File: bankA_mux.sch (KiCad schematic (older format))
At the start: 6 parts, among them U10 SHIFTER, U9 74HC4051

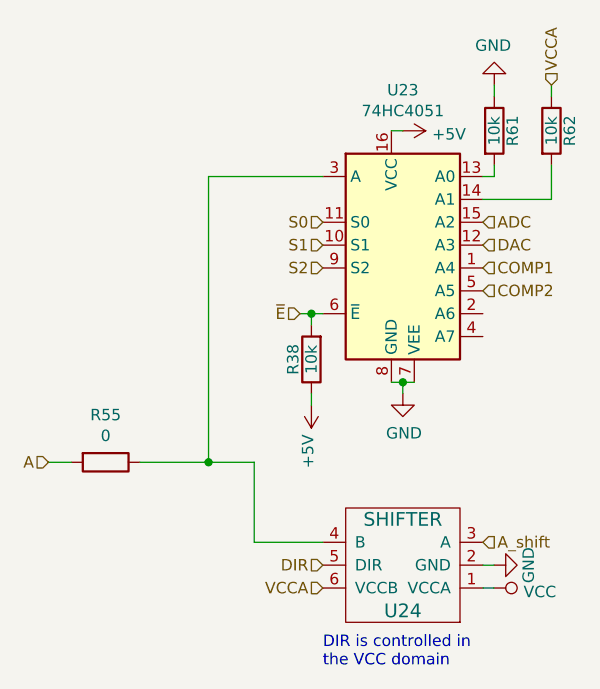
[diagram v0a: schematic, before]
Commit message: Changed headers for bank A and B, combined ADC voltage divider / pull-ups
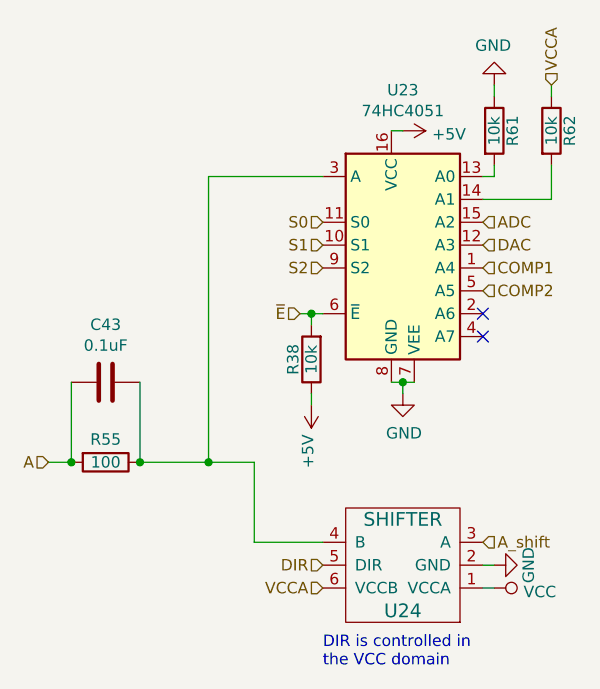
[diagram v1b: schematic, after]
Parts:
- added C39: 0.1uF, gsg-modules:0402, symbol Device:C
- R48: value 0 -> 100; Description (none) -> RES 100 OHM 5% 1/16W 0402; Manufacturer (none) -> Stackpole Electronics Inc; Part Number (none) -> RMCF0402JT100R
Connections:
- net A: now also C39.1
- net at R48.1, U10.4 (B), U9.3 (A): now also C39.2
- no-connect marks 0 -> 2
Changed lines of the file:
@@
 $Descr A4 11693 8268
 encoding utf-8
-Sheet 4 9
+Sheet 5 10
 Title ""
 Date ""
@@
 AR Path="/5D190D22/5CB0C423" Ref="R51"  Part="1"
 AR Path="/5D1A466A/5CB0C423" Ref="R53"  Part="1"
-F 0 "R55" V 2593 3700 50  0000 C CNN
-F 1 "0" V 2684 3700 50  0000 C CNN
+F 0 "R55" V 2700 3700 50  0000 C CNN
+F 1 "100" V 2800 3700 50  0000 C CNN
 F 2 "gsg-modules:0402" V 2730 3700 50  0001 C CNN
 F 3 "~" H 2800 3700 50  0001 C CNN
+F 4 "Stackpole Electronics Inc" H 2800 3700 50  0001 C CNN "Manufacturer"
+F 5 "RMCF0402JT100R" H 2800 3700 50  0001 C CNN "Part Number"
+F 6 "RES 100 OHM 5% 1/16W 0402" H 2800 3700 50  0001 C CNN "Description"
 	1    2800 3700
 	0    1    1    0
@@
 	1    0    0    -1
 $EndComp
+NoConn ~ 4450 3050
+NoConn ~ 4450 3150
+$Comp
+L Device:C C39
+U 1 1 5D112AA5
+P 2800 3350
+AR Path="/5D190D22/5D112AA5" Ref="C39"  Part="1"
+AR Path="/5D1A466A/5D112AA5" Ref="C41"  Part="1"
+AR Path="/5D190D0C/5D112AA5" Ref="C38"  Part="1"
+AR Path="/5CF421CD/5D112AA5" Ref="C20"  Part="1"
+AR Path="/5D17D622/5D112AA5" Ref="C37"  Part="1"
+AR Path="/5D1A4654/5D112AA5" Ref="C40"  Part="1"
+AR Path="/5D1A4680/5D112AA5" Ref="C42"  Part="1"
+AR Path="/5D1A4696/5D112AA5" Ref="C43"  Part="1"
+F 0 "C43" V 3052 3350 50  0000 C CNN
+F 1 "0.1uF" V 2961 3350 50  0000 C CNN
+F 2 "gsg-modules:0402" H 2838 3200 50  0001 C CNN
+F 3 "~" H 2800 3350 50  0001 C CNN
+F 4 "Taiyo Yuden" H 2800 3350 50  0001 C CNN "Manufacturer"
+F 5 "EMK105BJ104KV-F" H 2800 3350 50  0001 C CNN "Part Number"
+F 6 "CAP CER 0.1UF 16V X5R 0402 " H 2800 3350 50  0001 C CNN "Description"
+	1    2800 3350
+	0    -1   -1   0
+$EndComp
+Wire Wire Line
+	2650 3700 2650 3350
+Connection ~ 2650 3700
+Wire Wire Line
+	2950 3350 2950 3700
+Connection ~ 2950 3700
 $EndSCHEMATC

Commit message: Completed routing of new connectors.
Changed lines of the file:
@@
 $Descr A4 11693 8268
 encoding utf-8
-Sheet 5 10
+Sheet 5 17
 Title ""
 Date ""
@@
 AR Path="/5D1A4680/5CF3E254" Ref="U21"  Part="1"
 AR Path="/5D1A4696/5CF3E254" Ref="U23"  Part="1"
-F 0 "U23" H 4100 3428 50  0000 C CNN
+F 0 "U11" H 4100 3428 50  0000 C CNN
 F 1 "74HC4051" H 4100 3337 50  0000 C CNN
 F 2 "Package_TO_SOT_SMD:SOT-763-1" H 4050 2350 50  0001 C CNN
@@
 AR Path="/5D1A4680/5CF3E25C" Ref="#PWR0180"  Part="1"
 AR Path="/5D1A4696/5CF3E25C" Ref="#PWR0186"  Part="1"
-F 0 "#PWR0186" H 4100 2100 50  0001 C CNN
+F 0 "#PWR0150" H 4100 2100 50  0001 C CNN
 F 1 "+5V" V 4115 2378 50  0000 L CNN
 F 2 "" H 4100 2250 50  0001 C CNN
@@
 AR Path="/5D1A4680/5CF3E263" Ref="#PWR0181"  Part="1"
 AR Path="/5D1A4696/5CF3E263" Ref="#PWR0187"  Part="1"
-F 0 "#PWR0187" H 4100 3150 50  0001 C CNN
+F 0 "#PWR0151" H 4100 3150 50  0001 C CNN
 F 1 "GND" H 4105 3227 50  0000 C CNN
 F 2 "" H 4100 3400 50  0001 C CNN
@@
 AR Path="/5D1A4680/5CF3E282" Ref="#PWR0182"  Part="1"
 AR Path="/5D1A4696/5CF3E282" Ref="#PWR0188"  Part="1"
-F 0 "#PWR0188" H 4500 1800 50  0001 C CNN
+F 0 "#PWR0152" H 4500 1800 50  0001 C CNN
 F 1 "GND" H 4505 1877 50  0000 C CNN
 F 2 "" H 4500 2050 50  0001 C CNN
@@
 AR Path="/5D1A4680/5CF3E28C" Ref="U22"  Part="1"
 AR Path="/5D1A4696/5CF3E28C" Ref="U24"  Part="1"
-F 0 "U24" H 4100 4350 60  0000 C CNN
+F 0 "U12" H 4100 4350 60  0000 C CNN
 F 1 "SHIFTER" H 4100 3950 60  0000 C CNN
 F 2 "gsg-modules:SOT363" H 4100 4150 60  0001 C CNN
@@
 AR Path="/5D1A4680/5CF3E293" Ref="#PWR0183"  Part="1"
 AR Path="/5D1A4696/5CF3E293" Ref="#PWR0189"  Part="1"
-F 0 "#PWR0189" H 4500 3900 50  0001 C CNN
+F 0 "#PWR0153" H 4500 3900 50  0001 C CNN
 F 1 "GND" H 4500 4000 50  0000 C CNN
 F 2 "" H 4500 4150 60  0000 C CNN
@@
 AR Path="/5D1A4680/5CF3E2A6" Ref="R35"  Part="1"
 AR Path="/5D1A4696/5CF3E2A6" Ref="R38"  Part="1"
-F 0 "R38" V 3780 3250 50  0000 C CNN
+F 0 "R20" V 3780 3250 50  0000 C CNN
 F 1 "10k" V 3700 3250 50  0000 C CNN
 F 2 "gsg-modules:0402" V 3630 3250 50  0001 C CNN
@@
 AR Path="/5D1A4680/5CF3E2B2" Ref="#PWR0184"  Part="1"
 AR Path="/5D1A4696/5CF3E2B2" Ref="#PWR0190"  Part="1"
-F 0 "#PWR0190" H 3700 3300 50  0001 C CNN
+F 0 "#PWR0154" H 3700 3300 50  0001 C CNN
 F 1 "+5V" V 3715 3578 50  0000 L CNN
 F 2 "" H 3700 3450 50  0001 C CNN
@@
 AR Path="/5D1A4680/5CF3E2B8" Ref="#PWR0185"  Part="1"
 AR Path="/5D1A4696/5CF3E2B8" Ref="#PWR0191"  Part="1"
-F 0 "#PWR0191" H 4500 4100 50  0001 C CNN
+F 0 "#PWR0155" H 4500 4100 50  0001 C CNN
 F 1 "VCC" V 4517 4378 50  0000 L CNN
 F 2 "" H 4500 4250 50  0001 C CNN
@@
 AR Path="/5D190D22/5CB0C423" Ref="R51"  Part="1"
 AR Path="/5D1A466A/5CB0C423" Ref="R53"  Part="1"
-F 0 "R55" V 2700 3700 50  0000 C CNN
+F 0 "R49" V 2700 3700 50  0000 C CNN
 F 1 "100" V 2800 3700 50  0000 C CNN
 F 2 "gsg-modules:0402" V 2730 3700 50  0001 C CNN
@@
 AR Path="/5D1A4680/5CDC112C" Ref="R47"  Part="1"
 AR Path="/5D1A4696/5CDC112C" Ref="R62"  Part="1"
-F 0 "R62" V 4830 2250 50  0000 C CNN
+F 0 "R28" V 4830 2250 50  0000 C CNN
 F 1 "10k" V 4750 2250 50  0000 C CNN
 F 2 "gsg-modules:0402" V 4680 2250 50  0001 C CNN
@@
 AR Path="/5D1A4680/5CDC1279" Ref="R46"  Part="1"
 AR Path="/5D1A4696/5CDC1279" Ref="R61"  Part="1"
-F 0 "R61" V 4580 2250 50  0000 C CNN
+F 0 "R27" V 4580 2250 50  0000 C CNN
 F 1 "10k" V 4500 2250 50  0000 C CNN
 F 2 "gsg-modules:0402" V 4430 2250 50  0001 C CNN
@@
 AR Path="/5D1A4680/5D112AA5" Ref="C42"  Part="1"
 AR Path="/5D1A4696/5D112AA5" Ref="C43"  Part="1"
-F 0 "C43" V 3052 3350 50  0000 C CNN
+F 0 "C37" V 3052 3350 50  0000 C CNN
 F 1 "0.1uF" V 2961 3350 50  0000 C CNN
 F 2 "gsg-modules:0402" H 2838 3200 50  0001 C CNN

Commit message: Completed Bank A mux routing.
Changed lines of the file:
@@
 AR Path="/5D1A4680/5CF3E254" Ref="U21"  Part="1"
 AR Path="/5D1A4696/5CF3E254" Ref="U23"  Part="1"
-F 0 "U11" H 4100 3428 50  0000 C CNN
+F 0 "U19" H 4100 3428 50  0000 C CNN
 F 1 "74HC4051" H 4100 3337 50  0000 C CNN
 F 2 "Package_TO_SOT_SMD:SOT-763-1" H 4050 2350 50  0001 C CNN
@@
 AR Path="/5D1A4680/5CF3E25C" Ref="#PWR0180"  Part="1"
 AR Path="/5D1A4696/5CF3E25C" Ref="#PWR0186"  Part="1"
-F 0 "#PWR0150" H 4100 2100 50  0001 C CNN
+F 0 "#PWR0186" H 4100 2100 50  0001 C CNN
 F 1 "+5V" V 4115 2378 50  0000 L CNN
 F 2 "" H 4100 2250 50  0001 C CNN
@@
 AR Path="/5D1A4680/5CF3E263" Ref="#PWR0181"  Part="1"
 AR Path="/5D1A4696/5CF3E263" Ref="#PWR0187"  Part="1"
-F 0 "#PWR0151" H 4100 3150 50  0001 C CNN
+F 0 "#PWR0187" H 4100 3150 50  0001 C CNN
 F 1 "GND" H 4105 3227 50  0000 C CNN
 F 2 "" H 4100 3400 50  0001 C CNN
@@
 AR Path="/5D1A4680/5CF3E282" Ref="#PWR0182"  Part="1"
 AR Path="/5D1A4696/5CF3E282" Ref="#PWR0188"  Part="1"
-F 0 "#PWR0152" H 4500 1800 50  0001 C CNN
+F 0 "#PWR0188" H 4500 1800 50  0001 C CNN
 F 1 "GND" H 4505 1877 50  0000 C CNN
 F 2 "" H 4500 2050 50  0001 C CNN
@@
 AR Path="/5D1A4680/5CF3E28C" Ref="U22"  Part="1"
 AR Path="/5D1A4696/5CF3E28C" Ref="U24"  Part="1"
-F 0 "U12" H 4100 4350 60  0000 C CNN
+F 0 "U20" H 4100 4350 60  0000 C CNN
 F 1 "SHIFTER" H 4100 3950 60  0000 C CNN
 F 2 "gsg-modules:SOT363" H 4100 4150 60  0001 C CNN
@@
 AR Path="/5D1A4680/5CF3E293" Ref="#PWR0183"  Part="1"
 AR Path="/5D1A4696/5CF3E293" Ref="#PWR0189"  Part="1"
-F 0 "#PWR0153" H 4500 3900 50  0001 C CNN
+F 0 "#PWR0189" H 4500 3900 50  0001 C CNN
 F 1 "GND" H 4500 4000 50  0000 C CNN
 F 2 "" H 4500 4150 60  0000 C CNN
@@
 AR Path="/5D1A4680/5CF3E2A6" Ref="R35"  Part="1"
 AR Path="/5D1A4696/5CF3E2A6" Ref="R38"  Part="1"
-F 0 "R20" V 3780 3250 50  0000 C CNN
+F 0 "R32" V 3780 3250 50  0000 C CNN
 F 1 "10k" V 3700 3250 50  0000 C CNN
 F 2 "gsg-modules:0402" V 3630 3250 50  0001 C CNN
@@
 AR Path="/5D1A4680/5CF3E2B2" Ref="#PWR0184"  Part="1"
 AR Path="/5D1A4696/5CF3E2B2" Ref="#PWR0190"  Part="1"
-F 0 "#PWR0154" H 3700 3300 50  0001 C CNN
+F 0 "#PWR0190" H 3700 3300 50  0001 C CNN
 F 1 "+5V" V 3715 3578 50  0000 L CNN
 F 2 "" H 3700 3450 50  0001 C CNN
@@
 AR Path="/5D1A4680/5CF3E2B8" Ref="#PWR0185"  Part="1"
 AR Path="/5D1A4696/5CF3E2B8" Ref="#PWR0191"  Part="1"
-F 0 "#PWR0155" H 4500 4100 50  0001 C CNN
+F 0 "#PWR0191" H 4500 4100 50  0001 C CNN
 F 1 "VCC" V 4517 4378 50  0000 L CNN
 F 2 "" H 4500 4250 50  0001 C CNN
@@
 AR Path="/5D190D22/5CB0C423" Ref="R51"  Part="1"
 AR Path="/5D1A466A/5CB0C423" Ref="R53"  Part="1"
-F 0 "R49" V 2700 3700 50  0000 C CNN
+F 0 "R53" V 2700 3700 50  0000 C CNN
 F 1 "100" V 2800 3700 50  0000 C CNN
 F 2 "gsg-modules:0402" V 2730 3700 50  0001 C CNN
@@
 AR Path="/5D1A4680/5CDC112C" Ref="R47"  Part="1"
 AR Path="/5D1A4696/5CDC112C" Ref="R62"  Part="1"
-F 0 "R28" V 4830 2250 50  0000 C CNN
+F 0 "R40" V 4830 2250 50  0000 C CNN
 F 1 "10k" V 4750 2250 50  0000 C CNN
 F 2 "gsg-modules:0402" V 4680 2250 50  0001 C CNN
@@
 AR Path="/5D1A4680/5CDC1279" Ref="R46"  Part="1"
 AR Path="/5D1A4696/5CDC1279" Ref="R61"  Part="1"
-F 0 "R27" V 4580 2250 50  0000 C CNN
+F 0 "R39" V 4580 2250 50  0000 C CNN
 F 1 "10k" V 4500 2250 50  0000 C CNN
 F 2 "gsg-modules:0402" V 4430 2250 50  0001 C CNN
@@
 AR Path="/5D1A4680/5D112AA5" Ref="C42"  Part="1"
 AR Path="/5D1A4696/5D112AA5" Ref="C43"  Part="1"
-F 0 "C37" V 3052 3350 50  0000 C CNN
+F 0 "C41" V 3052 3350 50  0000 C CNN
 F 1 "0.1uF" V 2961 3350 50  0000 C CNN
 F 2 "gsg-modules:0402" H 2838 3200 50  0001 C CNN

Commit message: Added I2C IO expander
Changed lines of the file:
@@
 AR Path="/5D1A4680/5CF3E254" Ref="U21"  Part="1"
 AR Path="/5D1A4696/5CF3E254" Ref="U23"  Part="1"
-F 0 "U19" H 4100 3428 50  0000 C CNN
+F 0 "U23" H 4100 3428 50  0000 C CNN
 F 1 "74HC4051" H 4100 3337 50  0000 C CNN
 F 2 "Package_TO_SOT_SMD:SOT-763-1" H 4050 2350 50  0001 C CNN
@@
 AR Path="/5D1A4680/5CF3E28C" Ref="U22"  Part="1"
 AR Path="/5D1A4696/5CF3E28C" Ref="U24"  Part="1"
-F 0 "U20" H 4100 4350 60  0000 C CNN
+F 0 "U24" H 4100 4350 60  0000 C CNN
 F 1 "SHIFTER" H 4100 3950 60  0000 C CNN
 F 2 "gsg-modules:SOT363" H 4100 4150 60  0001 C CNN
@@
 AR Path="/5D1A4680/5CF3E2A6" Ref="R35"  Part="1"
 AR Path="/5D1A4696/5CF3E2A6" Ref="R38"  Part="1"
-F 0 "R32" V 3780 3250 50  0000 C CNN
+F 0 "R38" V 3780 3250 50  0000 C CNN
 F 1 "10k" V 3700 3250 50  0000 C CNN
 F 2 "gsg-modules:0402" V 3630 3250 50  0001 C CNN
@@
 AR Path="/5D190D22/5CB0C423" Ref="R51"  Part="1"
 AR Path="/5D1A466A/5CB0C423" Ref="R53"  Part="1"
-F 0 "R53" V 2700 3700 50  0000 C CNN
+F 0 "R55" V 2700 3700 50  0000 C CNN
 F 1 "100" V 2800 3700 50  0000 C CNN
 F 2 "gsg-modules:0402" V 2730 3700 50  0001 C CNN
@@
 AR Path="/5D1A4680/5CDC112C" Ref="R47"  Part="1"
 AR Path="/5D1A4696/5CDC112C" Ref="R62"  Part="1"
-F 0 "R40" V 4830 2250 50  0000 C CNN
+F 0 "R62" V 4830 2250 50  0000 C CNN
 F 1 "10k" V 4750 2250 50  0000 C CNN
 F 2 "gsg-modules:0402" V 4680 2250 50  0001 C CNN
@@
 AR Path="/5D1A4680/5CDC1279" Ref="R46"  Part="1"
 AR Path="/5D1A4696/5CDC1279" Ref="R61"  Part="1"
-F 0 "R39" V 4580 2250 50  0000 C CNN
+F 0 "R61" V 4580 2250 50  0000 C CNN
 F 1 "10k" V 4500 2250 50  0000 C CNN
 F 2 "gsg-modules:0402" V 4430 2250 50  0001 C CNN
@@
 AR Path="/5D1A4680/5D112AA5" Ref="C42"  Part="1"
 AR Path="/5D1A4696/5D112AA5" Ref="C43"  Part="1"
-F 0 "C41" V 3052 3350 50  0000 C CNN
+F 0 "C43" V 3052 3350 50  0000 C CNN
 F 1 "0.1uF" V 2961 3350 50  0000 C CNN
 F 2 "gsg-modules:0402" H 2838 3200 50  0001 C CNN

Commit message: Completed routing
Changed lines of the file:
@@
 AR Path="/5D1A4680/5CF3E254" Ref="U21"  Part="1"
 AR Path="/5D1A4696/5CF3E254" Ref="U23"  Part="1"
-F 0 "U23" H 4100 3428 50  0000 C CNN
+F 0 "U9" H 4100 3428 50  0000 C CNN
 F 1 "74HC4051" H 4100 3337 50  0000 C CNN
 F 2 "Package_TO_SOT_SMD:SOT-763-1" H 4050 2350 50  0001 C CNN
@@
 AR Path="/5D1A4680/5CF3E25C" Ref="#PWR0180"  Part="1"
 AR Path="/5D1A4696/5CF3E25C" Ref="#PWR0186"  Part="1"
-F 0 "#PWR0186" H 4100 2100 50  0001 C CNN
+F 0 "#PWR0144" H 4100 2100 50  0001 C CNN
 F 1 "+5V" V 4115 2378 50  0000 L CNN
 F 2 "" H 4100 2250 50  0001 C CNN
@@
 AR Path="/5D1A4680/5CF3E263" Ref="#PWR0181"  Part="1"
 AR Path="/5D1A4696/5CF3E263" Ref="#PWR0187"  Part="1"
-F 0 "#PWR0187" H 4100 3150 50  0001 C CNN
+F 0 "#PWR0145" H 4100 3150 50  0001 C CNN
 F 1 "GND" H 4105 3227 50  0000 C CNN
 F 2 "" H 4100 3400 50  0001 C CNN
@@
 AR Path="/5D1A4680/5CF3E282" Ref="#PWR0182"  Part="1"
 AR Path="/5D1A4696/5CF3E282" Ref="#PWR0188"  Part="1"
-F 0 "#PWR0188" H 4500 1800 50  0001 C CNN
+F 0 "#PWR0146" H 4500 1800 50  0001 C CNN
 F 1 "GND" H 4505 1877 50  0000 C CNN
 F 2 "" H 4500 2050 50  0001 C CNN
@@
 AR Path="/5D1A4680/5CF3E28C" Ref="U22"  Part="1"
 AR Path="/5D1A4696/5CF3E28C" Ref="U24"  Part="1"
-F 0 "U24" H 4100 4350 60  0000 C CNN
+F 0 "U10" H 4100 4350 60  0000 C CNN
 F 1 "SHIFTER" H 4100 3950 60  0000 C CNN
 F 2 "gsg-modules:SOT363" H 4100 4150 60  0001 C CNN
@@
 AR Path="/5D1A4680/5CF3E293" Ref="#PWR0183"  Part="1"
 AR Path="/5D1A4696/5CF3E293" Ref="#PWR0189"  Part="1"
-F 0 "#PWR0189" H 4500 3900 50  0001 C CNN
+F 0 "#PWR0147" H 4500 3900 50  0001 C CNN
 F 1 "GND" H 4500 4000 50  0000 C CNN
 F 2 "" H 4500 4150 60  0000 C CNN
@@
 AR Path="/5D1A4680/5CF3E2A6" Ref="R35"  Part="1"
 AR Path="/5D1A4696/5CF3E2A6" Ref="R38"  Part="1"
-F 0 "R38" V 3780 3250 50  0000 C CNN
+F 0 "R17" V 3780 3250 50  0000 C CNN
 F 1 "10k" V 3700 3250 50  0000 C CNN
 F 2 "gsg-modules:0402" V 3630 3250 50  0001 C CNN
@@
 AR Path="/5D1A4680/5CF3E2B2" Ref="#PWR0184"  Part="1"
 AR Path="/5D1A4696/5CF3E2B2" Ref="#PWR0190"  Part="1"
-F 0 "#PWR0190" H 3700 3300 50  0001 C CNN
+F 0 "#PWR0148" H 3700 3300 50  0001 C CNN
 F 1 "+5V" V 3715 3578 50  0000 L CNN
 F 2 "" H 3700 3450 50  0001 C CNN
@@
 AR Path="/5D1A4680/5CF3E2B8" Ref="#PWR0185"  Part="1"
 AR Path="/5D1A4696/5CF3E2B8" Ref="#PWR0191"  Part="1"
-F 0 "#PWR0191" H 4500 4100 50  0001 C CNN
+F 0 "#PWR0149" H 4500 4100 50  0001 C CNN
 F 1 "VCC" V 4517 4378 50  0000 L CNN
 F 2 "" H 4500 4250 50  0001 C CNN
@@
 AR Path="/5D190D22/5CB0C423" Ref="R51"  Part="1"
 AR Path="/5D1A466A/5CB0C423" Ref="R53"  Part="1"
-F 0 "R55" V 2700 3700 50  0000 C CNN
+F 0 "R48" V 2700 3700 50  0000 C CNN
 F 1 "100" V 2800 3700 50  0000 C CNN
 F 2 "gsg-modules:0402" V 2730 3700 50  0001 C CNN
@@
 AR Path="/5D1A4680/5CDC112C" Ref="R47"  Part="1"
 AR Path="/5D1A4696/5CDC112C" Ref="R62"  Part="1"
-F 0 "R62" V 4830 2250 50  0000 C CNN
+F 0 "R25" V 4830 2250 50  0000 C CNN
 F 1 "10k" V 4750 2250 50  0000 C CNN
 F 2 "gsg-modules:0402" V 4680 2250 50  0001 C CNN
@@
 AR Path="/5D1A4680/5CDC1279" Ref="R46"  Part="1"
 AR Path="/5D1A4696/5CDC1279" Ref="R61"  Part="1"
-F 0 "R61" V 4580 2250 50  0000 C CNN
+F 0 "R24" V 4580 2250 50  0000 C CNN
 F 1 "10k" V 4500 2250 50  0000 C CNN
 F 2 "gsg-modules:0402" V 4430 2250 50  0001 C CNN
@@
 AR Path="/5D1A4680/5D112AA5" Ref="C42"  Part="1"
 AR Path="/5D1A4696/5D112AA5" Ref="C43"  Part="1"
-F 0 "C43" V 3052 3350 50  0000 C CNN
+F 0 "C20" V 3052 3350 50  0000 C CNN
 F 1 "0.1uF" V 2961 3350 50  0000 C CNN
 F 2 "gsg-modules:0402" H 2838 3200 50  0001 C CNN

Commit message: Matched path length of bank B differential pairs
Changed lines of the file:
@@
 AR Path="/5D1A4680/5CF3E254" Ref="U21"  Part="1"
 AR Path="/5D1A4696/5CF3E254" Ref="U23"  Part="1"
-F 0 "U9" H 4100 3428 50  0000 C CNN
+F 0 "U21" H 4100 3428 50  0000 C CNN
 F 1 "74HC4051" H 4100 3337 50  0000 C CNN
 F 2 "Package_TO_SOT_SMD:SOT-763-1" H 4050 2350 50  0001 C CNN
@@
 AR Path="/5D1A4680/5CF3E25C" Ref="#PWR0180"  Part="1"
 AR Path="/5D1A4696/5CF3E25C" Ref="#PWR0186"  Part="1"
-F 0 "#PWR0144" H 4100 2100 50  0001 C CNN
+F 0 "#PWR0180" H 4100 2100 50  0001 C CNN
 F 1 "+5V" V 4115 2378 50  0000 L CNN
 F 2 "" H 4100 2250 50  0001 C CNN
@@
 AR Path="/5D1A4680/5CF3E263" Ref="#PWR0181"  Part="1"
 AR Path="/5D1A4696/5CF3E263" Ref="#PWR0187"  Part="1"
-F 0 "#PWR0145" H 4100 3150 50  0001 C CNN
+F 0 "#PWR0181" H 4100 3150 50  0001 C CNN
 F 1 "GND" H 4105 3227 50  0000 C CNN
 F 2 "" H 4100 3400 50  0001 C CNN
@@
 AR Path="/5D1A4680/5CF3E282" Ref="#PWR0182"  Part="1"
 AR Path="/5D1A4696/5CF3E282" Ref="#PWR0188"  Part="1"
-F 0 "#PWR0146" H 4500 1800 50  0001 C CNN
+F 0 "#PWR0182" H 4500 1800 50  0001 C CNN
 F 1 "GND" H 4505 1877 50  0000 C CNN
 F 2 "" H 4500 2050 50  0001 C CNN
@@
 AR Path="/5D1A4680/5CF3E28C" Ref="U22"  Part="1"
 AR Path="/5D1A4696/5CF3E28C" Ref="U24"  Part="1"
-F 0 "U10" H 4100 4350 60  0000 C CNN
+F 0 "U22" H 4100 4350 60  0000 C CNN
 F 1 "SHIFTER" H 4100 3950 60  0000 C CNN
 F 2 "gsg-modules:SOT363" H 4100 4150 60  0001 C CNN
@@
 AR Path="/5D1A4680/5CF3E293" Ref="#PWR0183"  Part="1"
 AR Path="/5D1A4696/5CF3E293" Ref="#PWR0189"  Part="1"
-F 0 "#PWR0147" H 4500 3900 50  0001 C CNN
+F 0 "#PWR0183" H 4500 3900 50  0001 C CNN
 F 1 "GND" H 4500 4000 50  0000 C CNN
 F 2 "" H 4500 4150 60  0000 C CNN
@@
 AR Path="/5D1A4680/5CF3E2A6" Ref="R35"  Part="1"
 AR Path="/5D1A4696/5CF3E2A6" Ref="R38"  Part="1"
-F 0 "R17" V 3780 3250 50  0000 C CNN
+F 0 "R35" V 3780 3250 50  0000 C CNN
 F 1 "10k" V 3700 3250 50  0000 C CNN
 F 2 "gsg-modules:0402" V 3630 3250 50  0001 C CNN
@@
 AR Path="/5D1A4680/5CF3E2B2" Ref="#PWR0184"  Part="1"
 AR Path="/5D1A4696/5CF3E2B2" Ref="#PWR0190"  Part="1"
-F 0 "#PWR0148" H 3700 3300 50  0001 C CNN
+F 0 "#PWR0184" H 3700 3300 50  0001 C CNN
 F 1 "+5V" V 3715 3578 50  0000 L CNN
 F 2 "" H 3700 3450 50  0001 C CNN
@@
 AR Path="/5D1A4680/5CF3E2B8" Ref="#PWR0185"  Part="1"
 AR Path="/5D1A4696/5CF3E2B8" Ref="#PWR0191"  Part="1"
-F 0 "#PWR0149" H 4500 4100 50  0001 C CNN
+F 0 "#PWR0185" H 4500 4100 50  0001 C CNN
 F 1 "VCC" V 4517 4378 50  0000 L CNN
 F 2 "" H 4500 4250 50  0001 C CNN
@@
 AR Path="/5D190D22/5CB0C423" Ref="R51"  Part="1"
 AR Path="/5D1A466A/5CB0C423" Ref="R53"  Part="1"
-F 0 "R48" V 2700 3700 50  0000 C CNN
+F 0 "R54" V 2700 3700 50  0000 C CNN
 F 1 "100" V 2800 3700 50  0000 C CNN
 F 2 "gsg-modules:0402" V 2730 3700 50  0001 C CNN
@@
 AR Path="/5D1A4680/5CDC112C" Ref="R47"  Part="1"
 AR Path="/5D1A4696/5CDC112C" Ref="R62"  Part="1"
-F 0 "R25" V 4830 2250 50  0000 C CNN
+F 0 "R47" V 4830 2250 50  0000 C CNN
 F 1 "10k" V 4750 2250 50  0000 C CNN
 F 2 "gsg-modules:0402" V 4680 2250 50  0001 C CNN
@@
 AR Path="/5D1A4680/5CDC1279" Ref="R46"  Part="1"
 AR Path="/5D1A4696/5CDC1279" Ref="R61"  Part="1"
-F 0 "R24" V 4580 2250 50  0000 C CNN
+F 0 "R46" V 4580 2250 50  0000 C CNN
 F 1 "10k" V 4500 2250 50  0000 C CNN
 F 2 "gsg-modules:0402" V 4430 2250 50  0001 C CNN
@@
 AR Path="/5D1A4680/5D112AA5" Ref="C42"  Part="1"
 AR Path="/5D1A4696/5D112AA5" Ref="C43"  Part="1"
-F 0 "C20" V 3052 3350 50  0000 C CNN
+F 0 "C42" V 3052 3350 50  0000 C CNN
 F 1 "0.1uF" V 2961 3350 50  0000 C CNN
 F 2 "gsg-modules:0402" H 2838 3200 50  0001 C CNN
